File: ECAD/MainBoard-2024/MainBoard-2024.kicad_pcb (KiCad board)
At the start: 2 copper layers, 100 x 100 mm, 60 parts, among them J1 XT60, J11 Conn_01x03, J12 Conn_01x04, J13 Conn_01x03, J14 Conn_01x03, J16 XT30, J17 XT30, J2 Conn_01x04, J20 BAU, J21 BAU, J22 Conn_01x04, J23 Conn_01x02, J26 BAU, J27 BAU, J28 Conn_01x02, J29 Conn_01x02, J3 ConStep1, J30 Conn_01x03, J5 ConStep1, J6 ConStep1, J7 XT30, J8 Conn_01x02, K2 FINDER-36.11, U1 Teensy3.5_All_Pins, U2 R-78B3.3-2.0, U3 R-78B12-2.0, U4 R-78B5.0-2.0

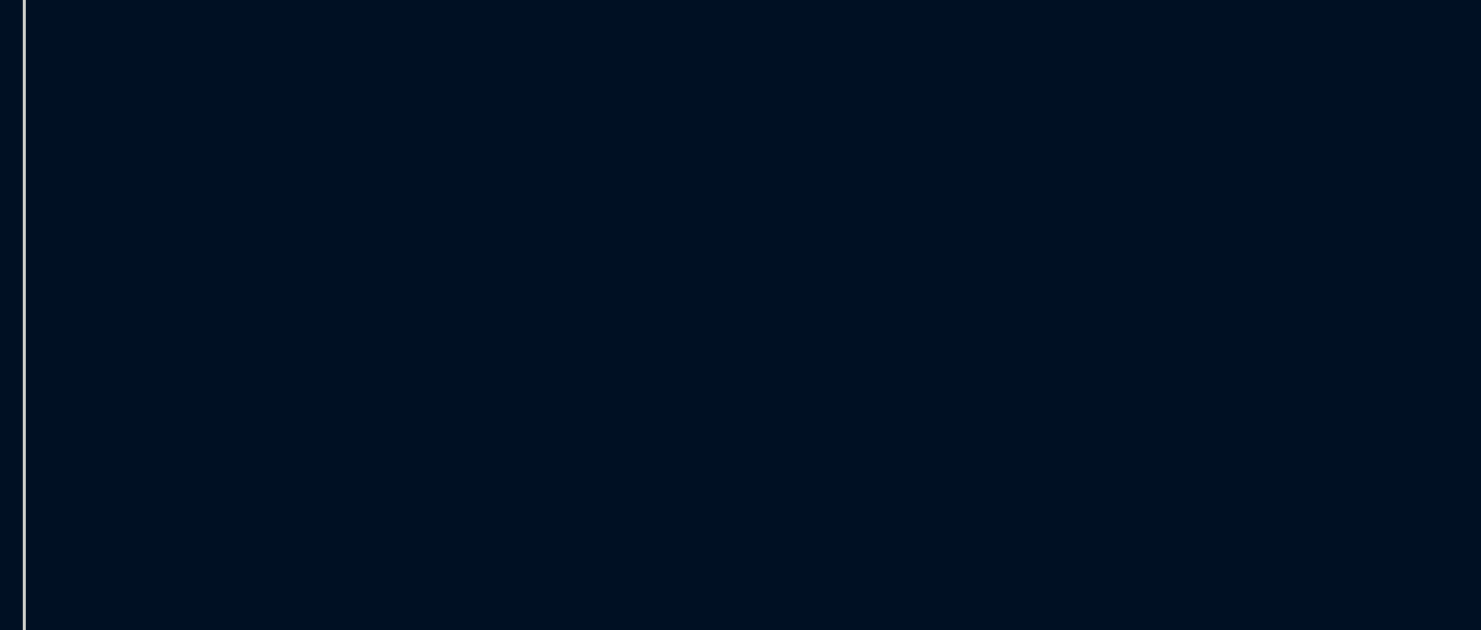
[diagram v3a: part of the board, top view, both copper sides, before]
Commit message: add ihm features and 12V connectores
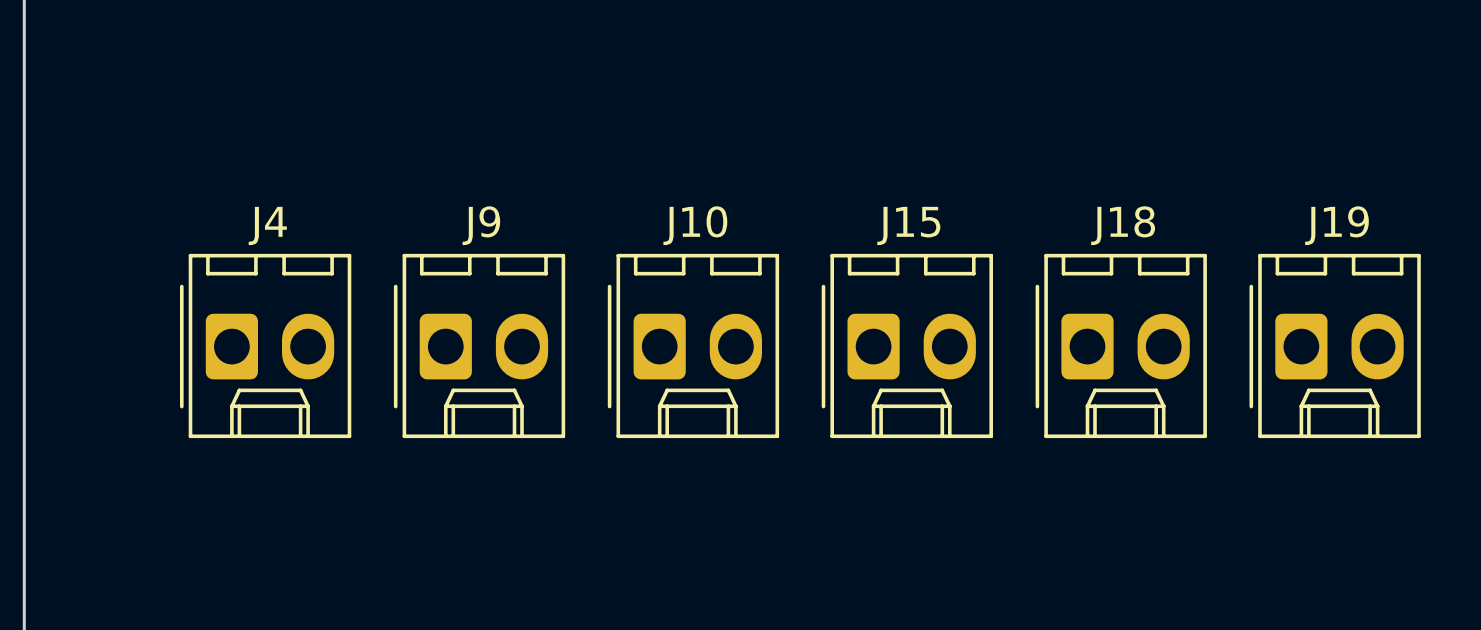
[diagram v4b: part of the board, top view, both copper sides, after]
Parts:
- added J10: Conn_01x02, Connector_Molex:Molex_KK-254_AE-6410-02A_1x02_P2.54mm_Vertical, F.Cu at (221.2, 96.5)
- added J15: Conn_01x02, Connector_Molex:Molex_KK-254_AE-6410-02A_1x02_P2.54mm_Vertical, F.Cu at (228.3, 96.5)
- added J18: Conn_01x02, Connector_Molex:Molex_KK-254_AE-6410-02A_1x02_P2.54mm_Vertical, F.Cu at (235.4, 96.5)
- added J19: Conn_01x02, Connector_Molex:Molex_KK-254_AE-6410-02A_1x02_P2.54mm_Vertical, F.Cu at (242.6, 96.5)
- added J4: Conn_01x02, Connector_Molex:Molex_KK-254_AE-6410-02A_1x02_P2.54mm_Vertical, F.Cu at (206.9, 96.5)
- added J9: Conn_01x02, Connector_Molex:Molex_KK-254_AE-6410-02A_1x02_P2.54mm_Vertical, F.Cu at (214.1, 96.5)
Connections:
- IHM-IO1 pad 1: unconnected-(IHM-IO1-Pin_1-Pad1) -> IHM_3
- IHM-IO1 pad 10: unconnected-(IHM-IO1-Pin_10-Pad10) -> DAC0
- IHM-IO1 pad 3: unconnected-(IHM-IO1-Pin_3-Pad3) -> IHM_4
- IHM-IO1 pad 4: unconnected-(IHM-IO1-Pin_4-Pad4) -> NEO_PIXEL
- IHM-IO1 pad 8: unconnected-(IHM-IO1-Pin_8-Pad8) -> DAC1
- J23 pad 1: +5V -> +12V
- J28 pad 1: +5V -> +12V
- J29 pad 1: +5V -> +12V
- U1 pad 21: unconnected-(U1-29_PWM_CAN0TX_Touch-Pad21) -> IHM_3
- U1 pad 22: unconnected-(U1-30_PWM_CAN0RX_Touch-Pad22) -> IHM_4
- U1 pad 37: unconnected-(U1-A21_DAC0-Pad37) -> DAC0
- U1 pad 38: unconnected-(U1-A22_DAC1-Pad38) -> DAC1
- U1 pad 40: unconnected-(U1-13_SCK0_LED-Pad40) -> En5VP

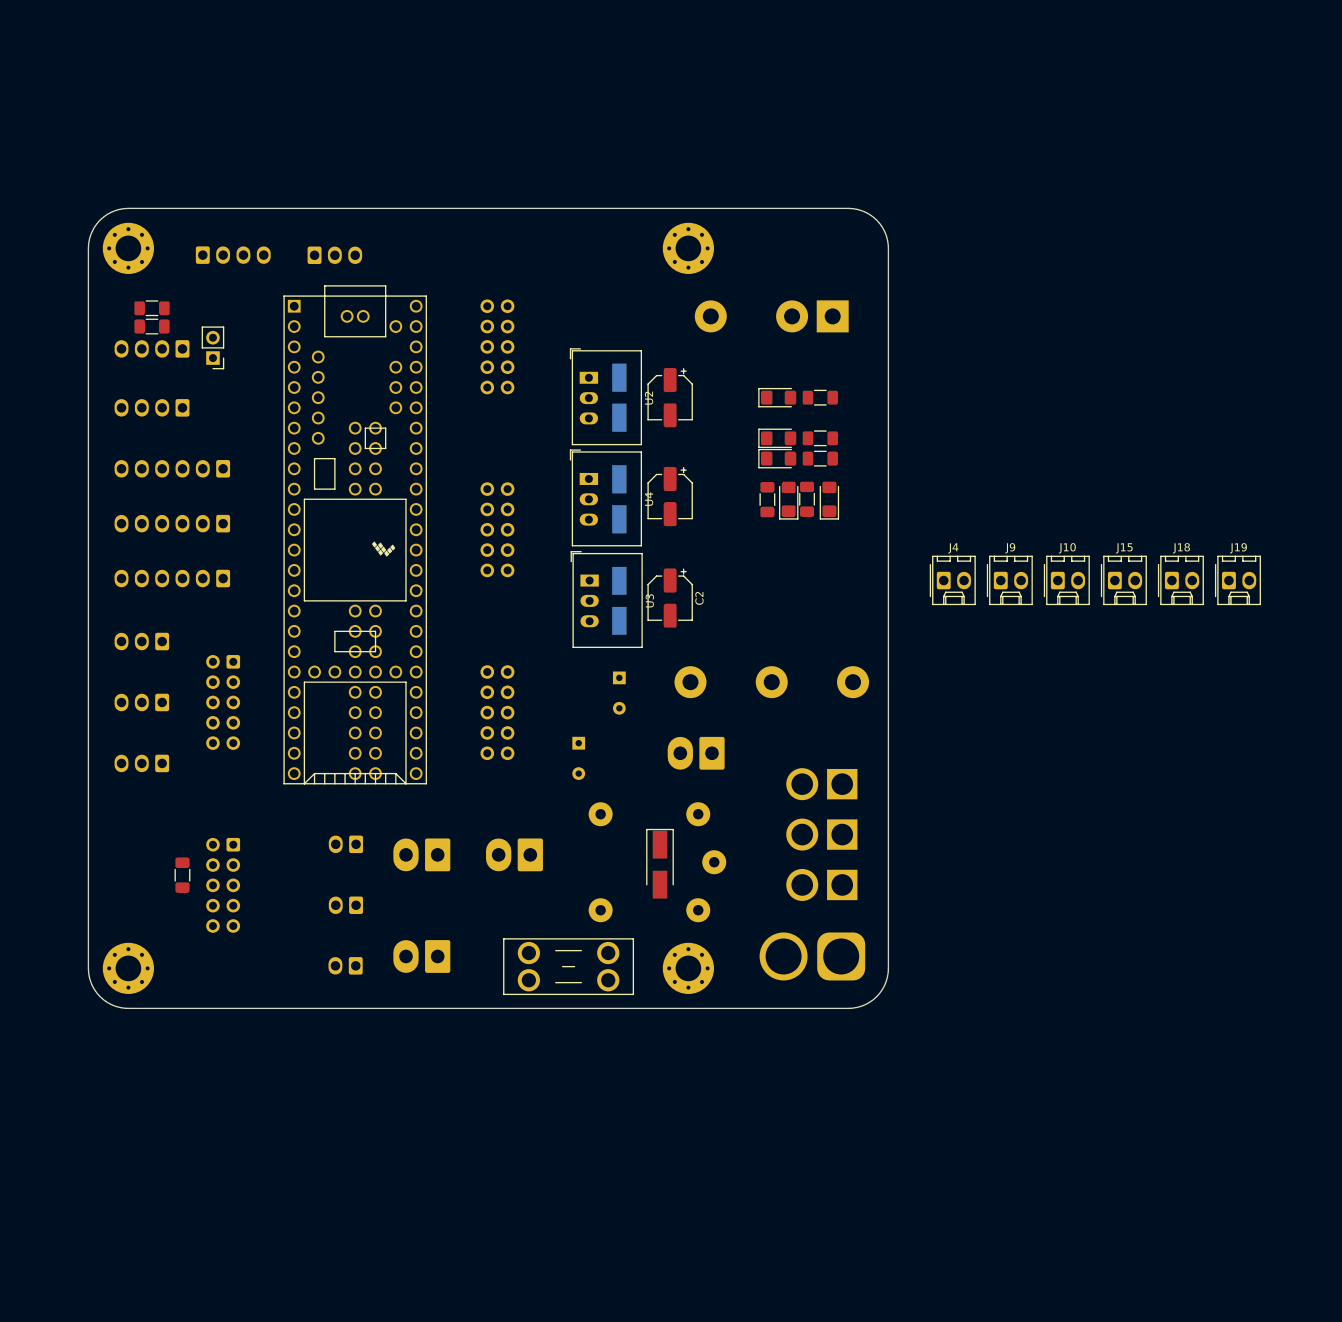
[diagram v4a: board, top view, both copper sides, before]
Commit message: Update 3.3V connectors and placements
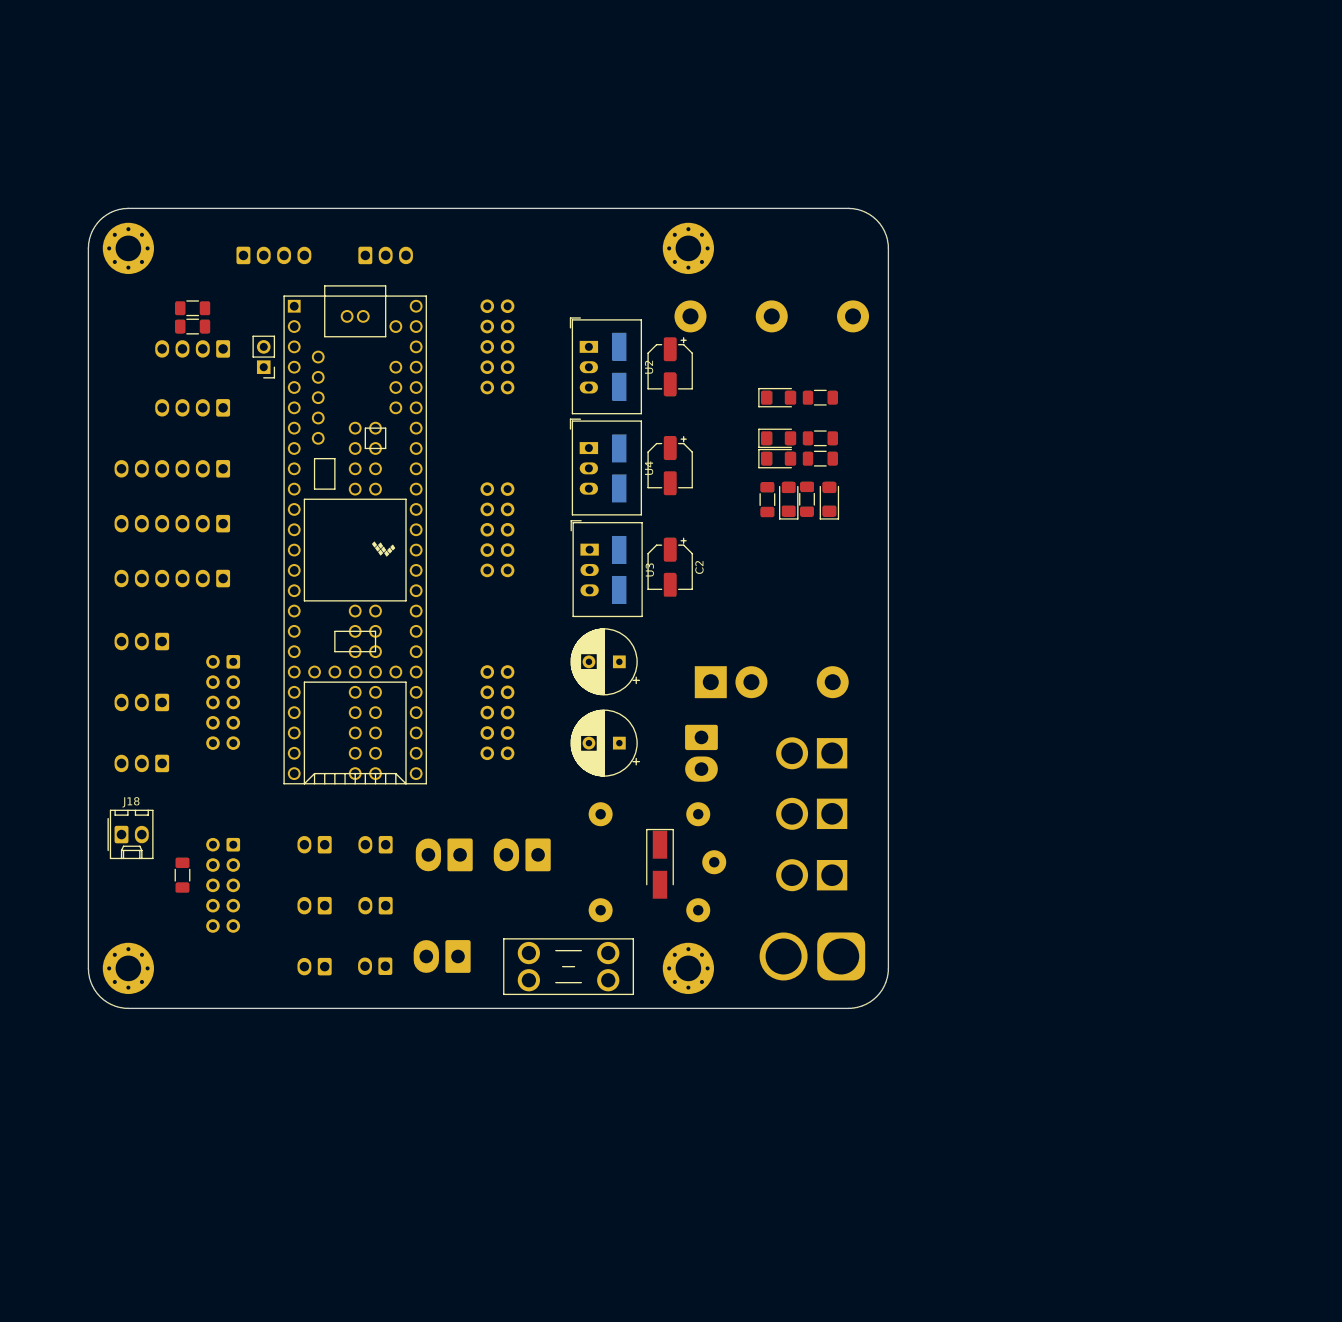
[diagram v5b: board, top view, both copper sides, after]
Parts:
- removed J15, J19: Conn_01x02, Connector_Molex:Molex_KK-254_AE-6410-02A_1x02_P2.54mm_Vertical
- C4, C6: moved to F.Cu
- J10, J4, J9: moved to B.Cu
- J18: value Conn_01x02 -> Tirette
- moved J18 135.1 mm to (104.1, 128.3)
- moved J10 103.6 mm to (129.5, 144.8), turned to 180 degrees
- moved J9 93.8 mm to (129.5, 137.2), turned to 180 degrees
- moved J4 84.1 mm to (129.5, 129.5), turned to 180 degrees
- moved J8 6.45 mm to (121.9, 69.8)
- moved J30 6.35 mm to (134.6, 55.9)
- moved J12 5.08 mm to (119.4, 55.9)
- moved C4 5.08 mm to (166.4, 116.8), turned to 180 degrees
- moved J2 5.08 mm to (116.8, 74.9)
- moved J22 5.08 mm to (116.8, 67.6)
- moved R21 5.08 mm to (113.0, 62.5)
- moved R22 5.08 mm to (113.0, 64.8)
- moved J16 4.06 mm to (193.0, 118.1)
- moved C1 3.86 mm to (172.7, 82.2)
- moved C2 3.86 mm to (172.7, 94.9)
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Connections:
- IHM-IO1 pad 9: Tirette -> +3V3
- J18 pad 1: +3V3 -> Tirette

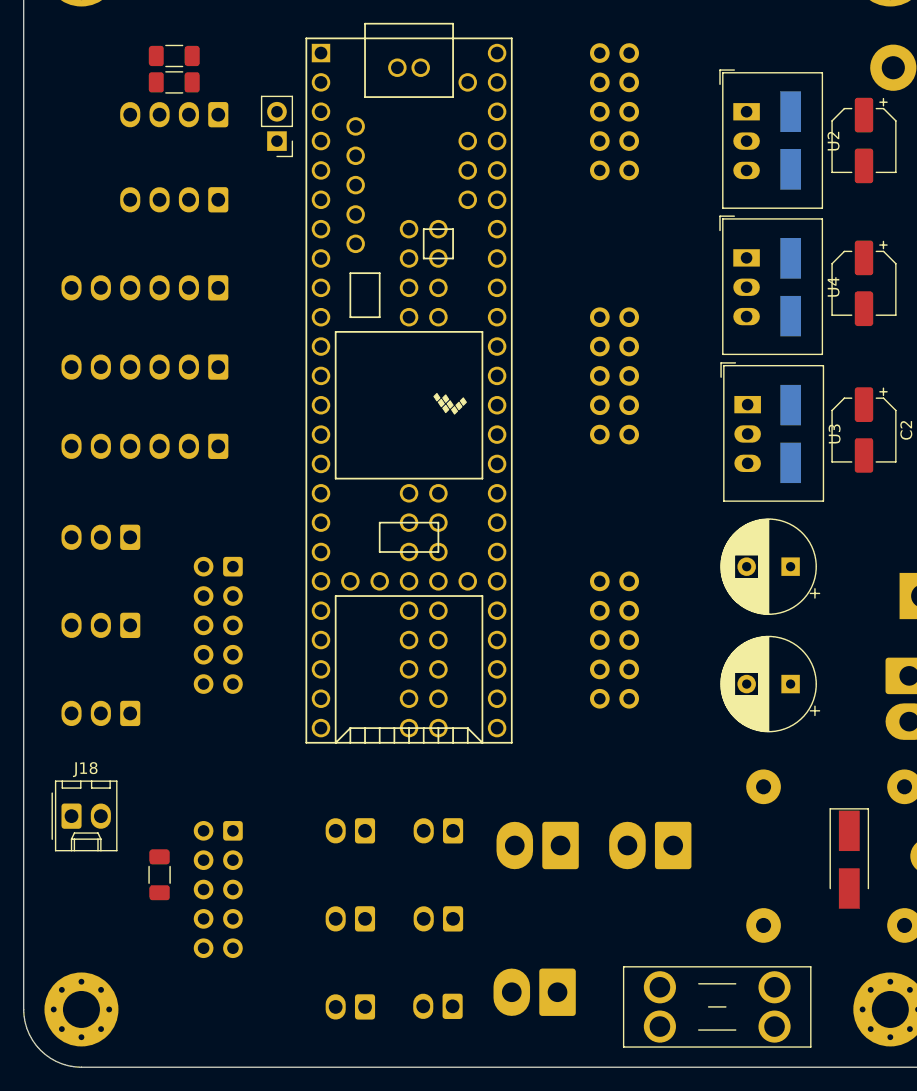
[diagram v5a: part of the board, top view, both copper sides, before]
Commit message: Generate 3D view
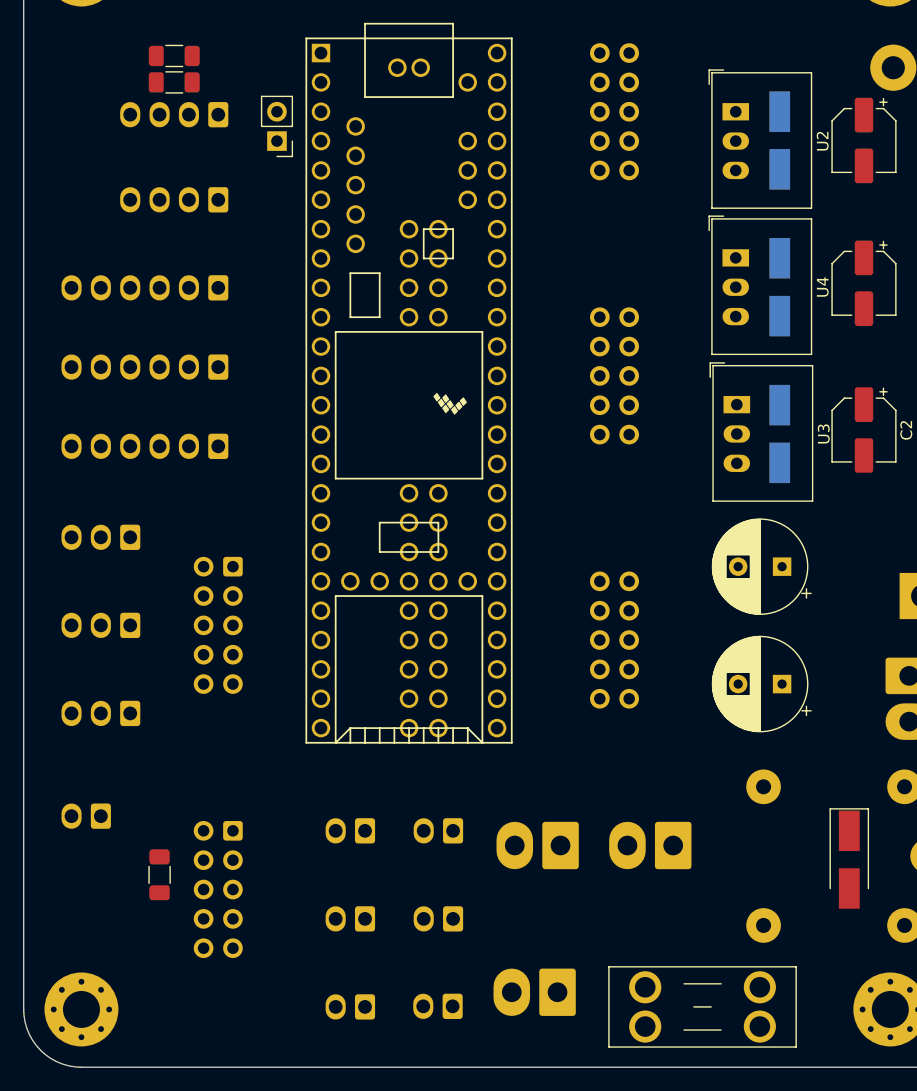
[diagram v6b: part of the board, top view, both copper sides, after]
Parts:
- J18: moved to B.Cu
- moved J18 2.54 mm to (106.7, 128.3), turned to 180 degrees
- moved F1 1.27 mm to (153.8, 143.1)
- moved D2 0.94 mm to (165.4, 82.5)
- moved D7 0.94 mm to (165.4, 69.8)
- moved D9 0.94 mm to (165.4, 95.2)
- moved U2 0.94 mm to (161.6, 67.3)
- moved U3 0.94 mm to (161.7, 92.7)
- moved U4 0.94 mm to (161.6, 80.0)
- moved C4 0.74 mm to (165.6, 116.8)
- moved C6 0.74 mm to (165.6, 106.7)
